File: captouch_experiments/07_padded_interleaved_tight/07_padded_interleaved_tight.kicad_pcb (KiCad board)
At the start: 2 copper layers, 227.9 x 66.5 mm, 3 parts, among them J1 Conn_01x08_Male, J2 Conn_01x32_Male, U1 captouch_8x32_grid

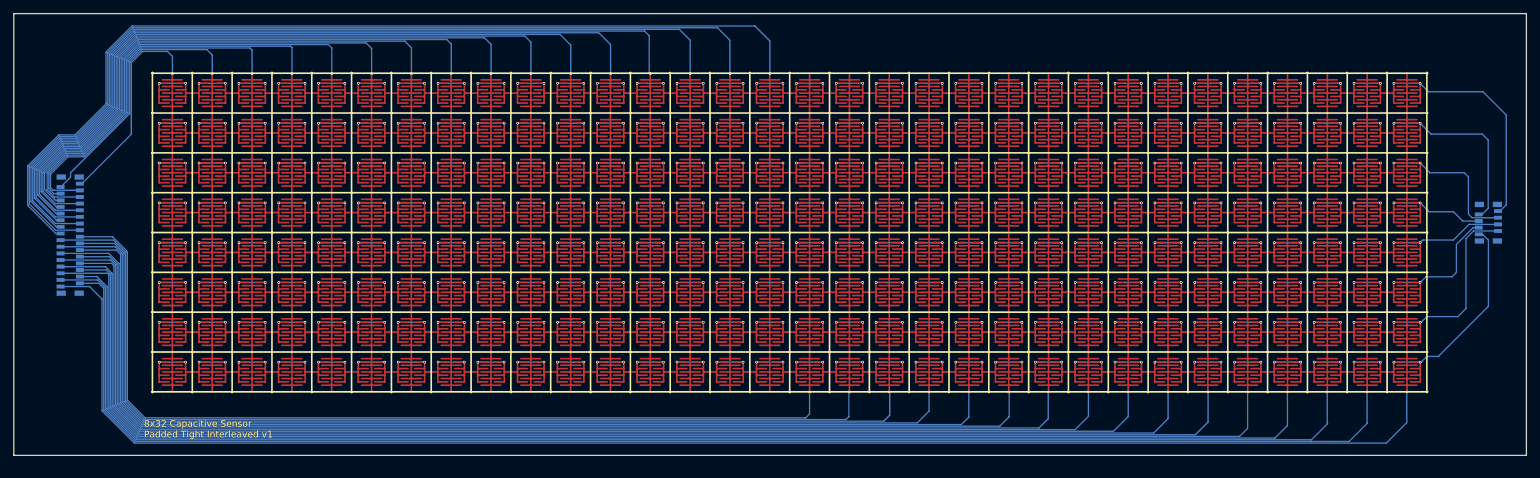
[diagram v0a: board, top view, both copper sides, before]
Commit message: added cap touch padded interleaved sensor boards
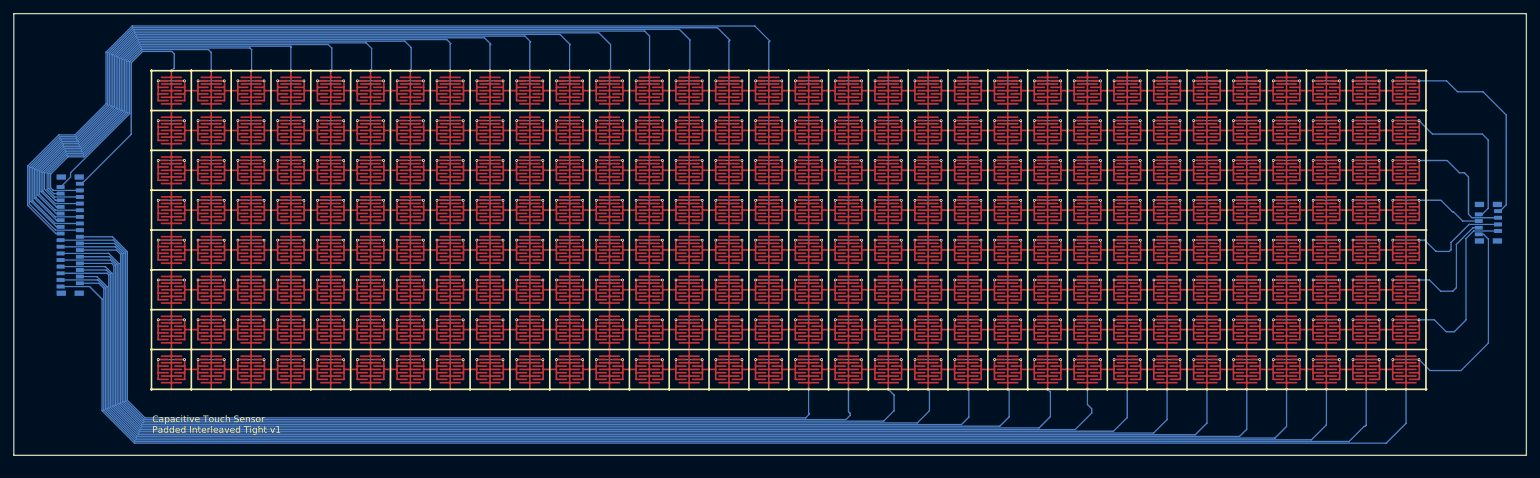
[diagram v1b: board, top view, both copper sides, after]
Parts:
- moved U1 0.40 mm to (62.8, 55.5)
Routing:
- net Net-(J1-Pad8): track 152.5 -> 156.7 mm
- net Net-(J1-Pad6): track 141.8 -> 143.9 mm
- net Net-(J1-Pad7): track 150.6 -> 152.5 mm
- net Net-(J1-Pad5): track 139.9 -> 141.3 mm
- net Net-(J2-Pad19): track 150.1 -> 151.1 mm
- net Net-(J2-Pad24): track 182.3 -> 183.2 mm
- net Net-(J2-Pad23): track 173.6 -> 174.3 mm
- net Net-(J2-Pad18): track 147.0 -> 147.6 mm
- net Net-(J2-Pad20): track 158.6 -> 159.1 mm
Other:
- board text added: "Capacitive Touch Sensor Padded Interleaved Tight v1"
- board text removed: "8x32 Capacitive Sensor Padded Tight Interleaved v1"

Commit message: added new high resolution touch boards
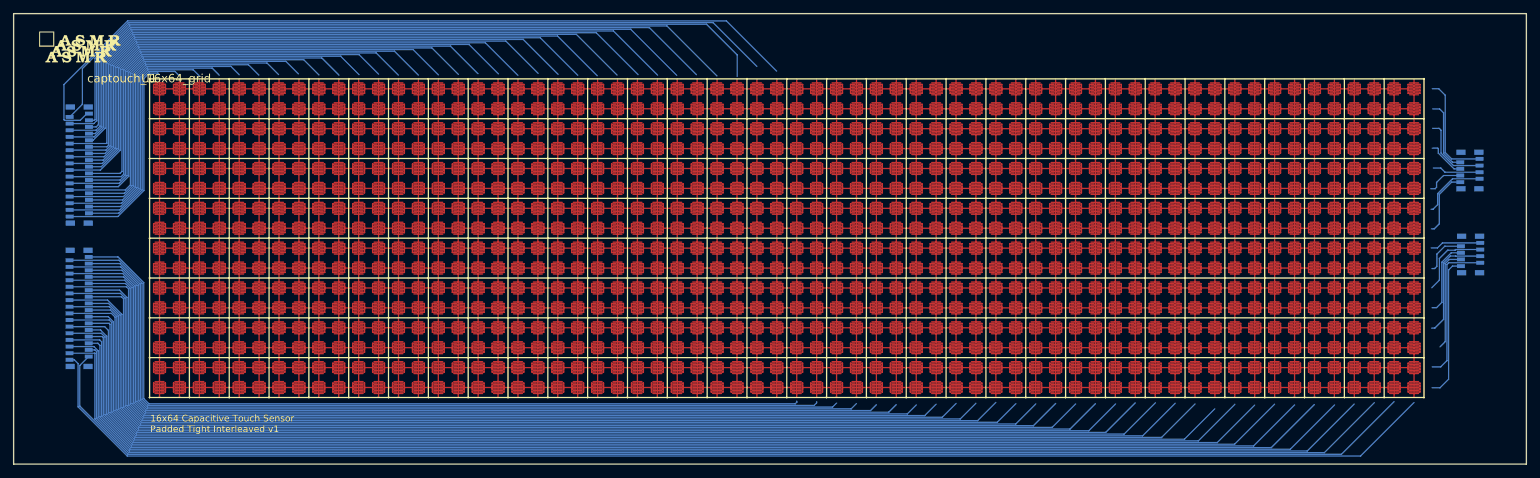
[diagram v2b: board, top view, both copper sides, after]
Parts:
- added G***: LOGO, ASMR_footprints:SilkScreen_asmrrrrrrrrr, F.Cu at (52.1, 52.3)
- added J3: Conn_01x08_Male, ASMR_footprints:Conn_FFC_1x8_0.5mm_Molex_5019510830, B.Cu at (261.5, 70.6)
- added J4: Conn_01x32_Male, ASMR_footprints:Conn_FFC_1x32_0.5mm_Molex_5019513210, B.Cu at (52.0, 69.8)
- J1: value Conn_01x08_Male -> Conn_01x32_Male; footprint ASMR_footprints:Conn_FFC_1x8_0.5mm_Molex_5019510830 -> ASMR_footprints:Conn_FFC_1x32_0.5mm_Molex_5019513210
- J2: value Conn_01x32_Male -> Conn_01x08_Male; footprint ASMR_footprints:Conn_FFC_1x32_0.5mm_Molex_5019513210 -> ASMR_footprints:Conn_FFC_1x8_0.5mm_Molex_5019510830
- U1: value captouch_8x32_grid -> captouch_16x64_grid; footprint ASMR_footprints:captouch_8x32_padded_interleaved -> ASMR_footprints:captouch_16x64_padded_interleaved_tight
- moved J1 212.7 mm to (52.0, 91.4), turned to 90 degrees
- moved J2 211.0 mm to (261.6, 83.3)
- moved U1 1.31 mm to (62.6, 56.8)
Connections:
- U1 pad 1: Net-(J1-Pad1) -> Net-(J3-Pad1)
- U1 pad 17: Net-(J2-Pad9) -> Net-(J4-Pad32)
- U1 pad 18: Net-(J2-Pad10) -> Net-(J4-Pad31)
- U1 pad 19: Net-(J2-Pad11) -> Net-(J4-Pad30)
- U1 pad 2: Net-(J1-Pad2) -> Net-(J3-Pad2)
- U1 pad 20: Net-(J2-Pad12) -> Net-(J4-Pad29)
- U1 pad 21: Net-(J2-Pad13) -> Net-(J4-Pad28)
- U1 pad 22: Net-(J2-Pad14) -> Net-(J4-Pad27)
- U1 pad 23: Net-(J2-Pad15) -> Net-(J4-Pad26)
- U1 pad 24: Net-(J2-Pad16) -> Net-(J4-Pad25)
- U1 pad 25: Net-(J2-Pad17) -> Net-(J4-Pad24)
- U1 pad 26: Net-(J2-Pad18) -> Net-(J4-Pad23)
- U1 pad 27: Net-(J2-Pad19) -> Net-(J4-Pad22)
- U1 pad 28: Net-(J2-Pad20) -> Net-(J4-Pad21)
- U1 pad 29: Net-(J2-Pad21) -> Net-(J4-Pad20)
- U1 pad 3: Net-(J1-Pad3) -> Net-(J3-Pad3)
- U1 pad 30: Net-(J2-Pad22) -> Net-(J4-Pad19)
- U1 pad 31: Net-(J2-Pad23) -> Net-(J4-Pad18)
- U1 pad 32: Net-(J2-Pad24) -> Net-(J4-Pad17)
- U1 pad 33: Net-(J2-Pad25) -> Net-(J4-Pad16)
- U1 pad 34: Net-(J2-Pad26) -> Net-(J4-Pad15)
- U1 pad 35: Net-(J2-Pad27) -> Net-(J4-Pad14)
- U1 pad 36: Net-(J2-Pad28) -> Net-(J4-Pad13)
- U1 pad 37: Net-(J2-Pad29) -> Net-(J4-Pad12)
- U1 pad 38: Net-(J2-Pad30) -> Net-(J4-Pad11)
- U1 pad 39: Net-(J2-Pad31) -> Net-(J4-Pad10)
- U1 pad 4: Net-(J1-Pad4) -> Net-(J3-Pad4)
- U1 pad 40: Net-(J2-Pad32) -> Net-(J4-Pad9)
- U1 pad 5: Net-(J1-Pad5) -> Net-(J3-Pad5)
- U1 pad 6: Net-(J1-Pad6) -> Net-(J3-Pad6)
- U1 pad 7: Net-(J1-Pad7) -> Net-(J3-Pad7)
- U1 pad 8: Net-(J1-Pad8) -> Net-(J3-Pad8)
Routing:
- net Net-(J2-Pad32): track 228.7 -> 0.00 mm, vias 1 -> 0
- net Net-(J2-Pad31): track 220.8 -> 0.00 mm, vias 1 -> 0
- net Net-(J2-Pad30): track 217.7 -> 0.00 mm, vias 1 -> 0
- net Net-(J2-Pad29): track 209.0 -> 0.00 mm, vias 1 -> 0
- net Net-(J2-Pad28): track 207.1 -> 0.00 mm, vias 1 -> 0
- net Net-(J2-Pad27): track 197.7 -> 0.00 mm, vias 1 -> 0
- net Net-(J1-Pad9): track 0.00 -> 194.6 mm
- net Net-(J2-Pad26): track 194.2 -> 0.00 mm, vias 1 -> 0
- net Net-(J1-Pad11): track 0.00 -> 188.8 mm
- net Net-(J1-Pad10): track 0.00 -> 188.8 mm
- net Net-(J2-Pad25): track 185.8 -> 0.00 mm, vias 1 -> 0
- net Net-(J1-Pad13): track 0.00 -> 183.7 mm
- net Net-(J1-Pad12): track 0.00 -> 183.7 mm
- net Net-(J2-Pad24): track 183.2 -> 0.00 mm, vias 1 -> 0
- net Net-(J1-Pad15): track 0.00 -> 178.1 mm
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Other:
- board size 227.9 x 66.5 mm -> 227.9 x 67.9 mm
- board text added: "16x64 Capacitive Touch Sensor Padded Tight Interleaved v1"
- board text removed: "Capacitive Touch Sensor Padded Interleaved Tight v1"
